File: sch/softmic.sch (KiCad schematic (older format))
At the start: 86 parts, among them J1 USB-C Connector, J2 XLR-OUT, J3 AudioJack 3.5mm, P1 4V1, P10 VccPad, P2 4V1, P3 4V1, P4 none, P5 none, P6 none, P7 none, P8 4V1, P9 4V1, Q1 MCP1812BT-033, Q10 ESP32-WROOM, Q11 BC847BS-TP, Q2 MMBFJ201, Q3 CH340G, Q4 BSS64AT116, Q5 OPA1671, Q6 OPA1671, Q7 BQ21040, Q8 MAX11613, Q9 Oled_128_32, SW1 RST, Y1 12MHz

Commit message: changed LED to red 0805 led
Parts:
- C1, C11, C12, C21, C22, C23, C24, C25, C3, C4, C5, C6, C7: Description CAP CER 1uF 10V X7R 0805 -> CAP CER 1uF 100V X7S 0805; MPN none -> HMK212BC7105MGHT; Manufacturer none -> Taiyo; Mouser PN none -> 963-HMK212BC7105MGHT; Mouser Price none -> $0.40
- C10, C14, C8: Description CAP CER 47uF 10V 0805 -> CAP CER 1206 10VDC 47uF 20% X6S; MPN none -> LMK316BC6476ML-T; Manufacturer none -> Taiyo; Mouser PN none -> 963-LMK316BC6476ML-T; Mouser Price none -> $0.70
- C13, C2, C9: Description CAP CER 22pF 10V X7R 0805 -> CAP CER 22pF 100V X7R 0805
- C15, C16: Description CAP CER 1uF 100V X7R 0805 -> CAP CER 1uF 100V X7S 0805; MPN none -> HMK212BC7105MGHT; Manufacturer none -> Taiyo; Mouser PN none -> 963-HMK212BC7105MGHT; Mouser Price none -> $0.40
- C19, C20: Description CAP CER 5.1nF 10V X7R 0805 -> CAP CER 5.1nF 100V X7R 0805
- D2: footprint LED_SMD:LED_0603_1608Metric -> LED_SMD:LED_0805_2012Metric_Pad1.15x1.40mm_HandSolder; Description LED Green 0603 SMD -> LED Red 0805 SMD; Digikey PN 511-1584-1-ND -> 732-4984-1-ND; Digikey Price $0.42 -> $0.18; LCSC PN C205443 -> (none); LCSC Price $0.008745 -> (none); MPN none -> Wurth; Manufacturer none -> 150080RS75000; Mouser PN 755-SMLD12EN1WT86 -> 710-150080RS75000; Mouser Price $0.40 -> $0.20

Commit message: pcb components placed
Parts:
- added C4: 1u, Capacitor_SMD:C_0805_2012Metric_Pad1.15x1.40mm_HandSolder, symbol Device:C
- logo1: footprint Symbol:OSHW-Logo2_7.3x6mm_SilkScreen -> Symbol:OSHW-Logo2_9.8x8mm_SilkScreen
- renumbered C9 to C10, C10 to C11, C11 to C12, C12 to C13, C13 to C14, C14 to C15, C15 to C16, C16 to C17, C17 to C18, C18 to C19, C19 to C20, C20 to C21, C21 to C22, C22 to C23, C23 to C24, C24 to C25, C25 to C26, C4 to C5, C5 to C6, C6 to C7, C7 to C8, C8 to C9, Q9 to DIS1
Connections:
- wire segments 251 -> 253
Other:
- moved on the sheet: C5

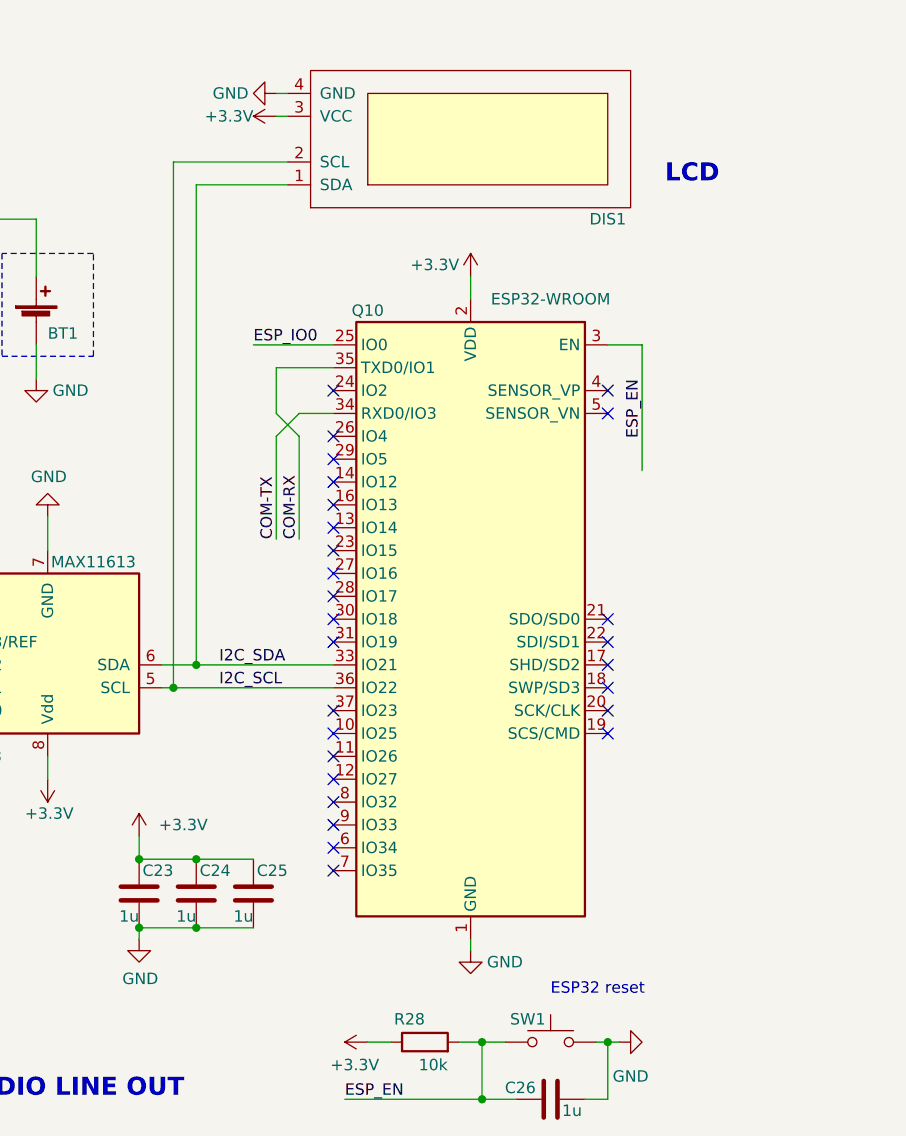
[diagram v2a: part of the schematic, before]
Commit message: changed ESP32 module for the 16MB version
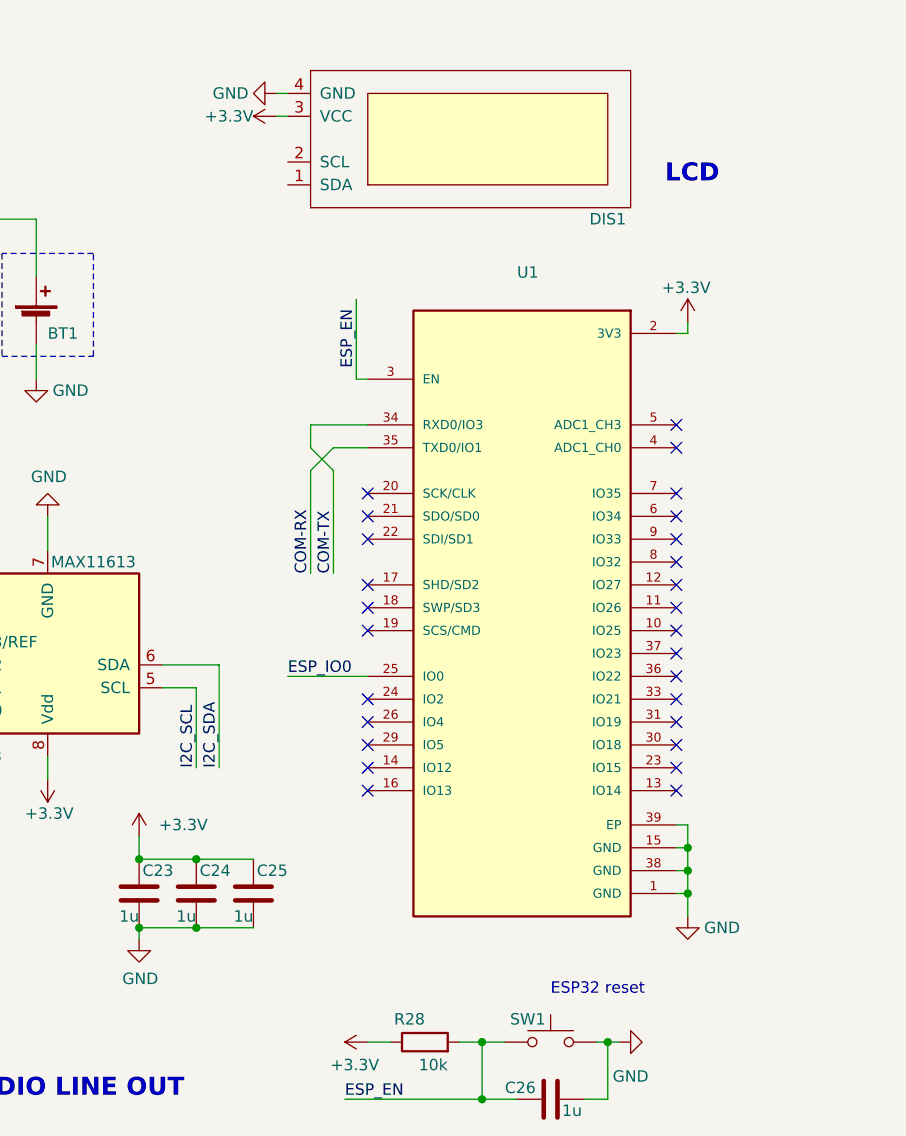
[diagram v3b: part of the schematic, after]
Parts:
- removed Q10: ESP32-WROOM, RF_Module:ESP32-WROOM-32, symbol RF_Module:ESP32-WROOM-32
- added U1: ESP32-WROVER-B 16MB, footprint:ESP32-WROVER-B_(16MB), symbol ESP32-WROVER-B.16MB:ESP32-WROVER-B_(16MB)
- Y1: Digikey Price (none) -> none; Mouser PN 717-AA-12.000MAGE-T -> 356-ESP32-WROB(16MB)
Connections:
- wire segments 253 -> 257
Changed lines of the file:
@@
 OP AMP 1\n
-$Comp
-L RF_Module:ESP32-WROOM-32 Q10
-U 1 1 5E8A3349
-P 9900 3050
-F 0 "Q10" H 10350 4400 50  0000 C CNN
-F 1 "ESP32-WROOM" H 9550 4450 50  0000 C CNN
-F 2 "RF_Module:ESP32-WROOM-32" H 9900 1550 50  0001 C CNN
-F 3 "https://www.espressif.com/sites/default/files/documentation/esp32-wroom-32_datasheet_en.pdf" H 9600 3100 50  0001 C CNN
-F 4 "Espressif Systems" H 9900 3050 50  0001 C CNN "Manufacturer"
-F 5 "ESP32-WROOM-32" H 9900 3050 50  0001 C CNN "MPN"
-F 6 "WiFi Modules (802.11) 4MB, ESP32-D0WDQ6" H 9900 3050 50  0001 C CNN "Description"
-F 7 "none" H 9900 3050 50  0001 C CNN "Digikey PN"
-F 8 "none" H 9900 3050 50  0001 C CNN "Digikey Price"
-F 9 "356-ESP-WROOM-32" H 9900 3050 50  0001 C CNN "Mouser PN"
-F 10 "$3.80" H 9900 3050 50  0001 C CNN "Mouser Price"
-F 11 "C95209" H 9900 3050 50  0001 C CNN "LCSC PN"
-F 12 "$2.79" H 9900 3050 50  0001 C CNN "LCSC Price"
-	1    9900 3050
-	-1   0    0    -1
-$EndComp
 $Comp
 L Device:C C21
@@
 L power:GND #PWR053
 U 1 1 5E85E862
-P 9900 4500
-F 0 "#PWR053" H 9900 4250 50  0001 C CNN
-F 1 "GND" H 9750 4450 50  0000 C CNN
-F 2 "" H 9900 4500 50  0001 C CNN
-F 3 "" H 9900 4500 50  0001 C CNN
-	1    9900 4500
+P 10850 4350
+F 0 "#PWR053" H 10850 4100 50  0001 C CNN
+F 1 "GND" H 10700 4300 50  0000 C CNN
+F 2 "" H 10850 4350 50  0001 C CNN
+F 3 "" H 10850 4350 50  0001 C CNN
+	1    10850 4350
 	-1   0    0    -1
 $EndComp
-Wire Wire Line
-	9900 4450 9900 4500
 $Comp
 L power:+3.3V #PWR052
 U 1 1 5E864686
-P 9900 1550
-F 0 "#PWR052" H 9900 1400 50  0001 C CNN
-F 1 "+3.3V" H 9950 1600 50  0000 L CNN
-F 2 "" H 9900 1550 50  0001 C CNN
-F 3 "" H 9900 1550 50  0001 C CNN
-	1    9900 1550
+P 10850 1750
+F 0 "#PWR052" H 10850 1600 50  0001 C CNN
+F 1 "+3.3V" H 10750 1900 50  0000 L CNN
+F 2 "" H 10850 1750 50  0001 C CNN
+F 3 "" H 10850 1750 50  0001 C CNN
+	1    10850 1750
 	-1   0    0    -1
 $EndComp
-Wire Wire Line
-	9900 1550 9900 1650
 Wire Wire Line
 	3400 6550 3300 6550
@@
 Wire Wire Line
 	8050 3750 8050 3650
-Text Label 8800 3350 0    50   ~ 0
+Text Label 8700 3700 1    50   ~ 0
 I2C_SCL
-Text Label 8800 3250 0    50   ~ 0
+Text Label 8800 3700 1    50   ~ 0
 I2C_SDA
 Wire Wire Line
@@
 Wire Wire Line
 	3950 4800 4300 4800
-NoConn ~ 9300 2050
-NoConn ~ 9300 2250
-NoConn ~ 9300 2350
-NoConn ~ 9300 2450
-NoConn ~ 9300 2650
-NoConn ~ 9300 2850
-NoConn ~ 9300 2950
-NoConn ~ 9300 3050
-NoConn ~ 9300 3150
-NoConn ~ 9300 3450
-NoConn ~ 9300 3550
-NoConn ~ 9300 3650
-NoConn ~ 9300 3750
-NoConn ~ 9300 3850
-NoConn ~ 9300 3950
-NoConn ~ 9300 4050
-NoConn ~ 9300 4150
-NoConn ~ 10500 3050
-NoConn ~ 10500 3150
-NoConn ~ 10500 3250
-NoConn ~ 10500 3350
-NoConn ~ 10500 3450
-NoConn ~ 10500 3550
-NoConn ~ 10500 2050
-NoConn ~ 10500 2150
 $Comp
 L Connector:XLR3 J2
@@
 Wire Wire Line
 	9100 750  9050 750
-Text Label 10650 2000 3    50   ~ 0
+Text Label 9400 1950 1    50   ~ 0
 ESP_EN
-NoConn ~ 9300 2750
-NoConn ~ 9300 2550
 $Comp
 L Switch:SW_Push SW1
@@
 	10500 5150 10500 4900
 Connection ~ 10500 4900
-Text Label 8950 1850 0    50   ~ 0
-ESP_IO0
-Wire Wire Line
-	8950 1850 9300 1850
-Wire Wire Line
-	10500 1850 10650 1850
+Wire Wire Line
+	9450 2000 9400 2000
 Wire Wire Line
 	3500 4800 3650 4800
@@
 Wire Wire Line
 	6950 3450 7550 3450
-Wire Wire Line
-	8600 1050 9100 1050
 Text Notes 10750 1150 0    79   ~ 16
 LCD\n
 Wire Wire Line
-	8550 3250 8700 3250
-Wire Wire Line
-	8550 3350 8600 3350
-Wire Wire Line
-	8700 3250 8700 1150
-Connection ~ 8700 3250
-Wire Wire Line
-	8700 3250 9300 3250
-Wire Wire Line
-	8700 1150 9100 1150
-Connection ~ 8600 3350
-Wire Wire Line
-	8600 3350 9300 3350
-Wire Wire Line
-	10650 1850 10650 2400
+	9400 2000 9400 1650
 Wire Wire Line
 	3300 4400 3800 4400
@@
 Text Label 3400 1150 0    50   ~ 0
 COM-TX
-Text Label 9150 2700 1    50   ~ 0
+Text Label 9200 2850 1    50   ~ 0
 COM-RX
-Text Label 9050 2700 1    50   ~ 0
+Text Label 9300 2850 1    50   ~ 0
 COM-TX
-Wire Wire Line
-	9300 2150 9150 2150
-Wire Wire Line
-	9300 1950 9050 1950
 Text Label 2900 3600 0    50   ~ 0
 JFET_OUT
@@
 	6850 6550 6850 7050
 Connection ~ 6050 6550
-Wire Wire Line
-	8600 1050 8600 3350
 Text Notes 7100 6850 0    79   ~ 16
 SOFTWARE-DEFINED WIRELESS MICROPHONE
@@
 ESP_EN
 Wire Wire Line
-	9150 2150 9050 2250
-Wire Wire Line
-	9050 2150 9150 2250
-Wire Wire Line
-	9050 1950 9050 2150
-Wire Wire Line
-	9150 2250 9150 2700
-Wire Wire Line
-	9050 2250 9050 2700
+	9300 2300 9200 2400
+Wire Wire Line
+	9200 2300 9300 2400
+Wire Wire Line
+	9200 2200 9200 2300
+Wire Wire Line
+	9300 2400 9300 2850
+Wire Wire Line
+	9200 2400 9200 2850
 Text Label 9300 5900 0    50   ~ 0
 RTS
@@
 F 7 "TCX Corporation" H 3800 2300 50  0001 C CNN "MPN"
 F 8 "AA-12.000MAGE-T " H 3800 2300 50  0001 C CNN "Manufacturer"
-F 9 "717-AA-12.000MAGE-T " H 3800 2300 50  0001 C CNN "Mouser PN"
+F 9 "356-ESP32-WROB(16MB) " H 3800 2300 50  0001 C CNN "Mouser PN"
 F 10 "$0.6" H 3800 2300 50  0001 C CNN "Mouser Price"
 F 11 " 887-1656-2-ND" H 3800 2300 50  0001 C CNN "Digikey PN"
+F 12 "none" H 3800 2300 50  0001 C CNN "Digikey Price"
 	1    3800 2300
 	1    0    0    -1
@@
 Wire Wire Line
 	2050 2350 2050 2300
+$Comp
+L ESP32-WROVER-B.16MB:ESP32-WROVER-B_(16MB) U1
+U 1 1 5EB184CB
+P 10150 3000
+F 0 "U1" H 10150 4467 50  0000 C CNN
+F 1 "ESP32-WROVER-B 16MB" V 10200 2250 50  0001 C CNN
+F 2 "footprint:ESP32-WROVER-B_(16MB)" H 10150 3000 50  0001 L BNN
+F 3 "https://eu.mouser.com/datasheet/2/891/esp32-wrover-b_datasheet_en-1384674.pdf" H 10150 3000 50  0001 L BNN
+F 4 "none" H 10150 3000 50  0001 C CNN "LCSC PN"
+F 5 "none" H 10150 3000 50  0001 C CNN "LCSC Price"
+F 6 "ESP32-WROVER-B (16MB)" H 10150 3000 50  0001 C CNN "MPN"
+F 7 "Espressif Systems" H 10150 3000 50  0001 C CNN "Manufacturer"
+F 8 "356-ESP32-WROB(16MB)" H 10150 3000 50  0001 C CNN "Mouser PN"
+F 9 "$4.80" H 10150 3000 50  0001 C CNN "Mouser Price"
+F 10 "ESP32 module M213DH2864PH3Q0, ESP32-D0WD, 64Mbits PSRAM, 16MB SPI flash, PCB Antenna" H 10150 3000 50  0001 C CNN "Description"
+F 11 "none" H 10150 3000 50  0001 C CNN "Digikey PN"
+F 12 "none" H 10150 3000 50  0001 C CNN "Digikey Price"
+	1    10150 3000
+	1    0    0    -1
+$EndComp
+Wire Wire Line
+	10800 1800 10850 1800
+Wire Wire Line
+	10850 1800 10850 1750
+Wire Wire Line
+	9450 2300 9300 2300
+Wire Wire Line
+	9450 2200 9200 2200
+Wire Wire Line
+	9100 3300 9450 3300
+Text Label 9100 3300 0    50   ~ 0
+ESP_IO0
+Wire Wire Line
+	10800 4250 10850 4250
+Wire Wire Line
+	10850 4250 10850 4350
+Wire Wire Line
+	10800 4150 10850 4150
+Wire Wire Line
+	10850 4150 10850 4250
+Connection ~ 10850 4250
+Wire Wire Line
+	10800 4050 10850 4050
+Wire Wire Line
+	10850 4050 10850 4150
+Connection ~ 10850 4150
+Wire Wire Line
+	10800 3950 10850 3950
+Wire Wire Line
+	10850 3950 10850 4050
+Connection ~ 10850 4050
+Wire Wire Line
+	8550 3350 8700 3350
+Wire Wire Line
+	8700 3350 8700 3700
+Wire Wire Line
+	8800 3250 8800 3700
+Wire Wire Line
+	8550 3250 8800 3250
+NoConn ~ 10800 2200
+NoConn ~ 10800 2300
+NoConn ~ 10800 2500
+NoConn ~ 10800 2600
+NoConn ~ 10800 2700
+NoConn ~ 10800 2800
+NoConn ~ 10800 2900
+NoConn ~ 10800 3000
+NoConn ~ 10800 3100
+NoConn ~ 10800 3200
+NoConn ~ 10800 3300
+NoConn ~ 10800 3400
+NoConn ~ 10800 3500
+NoConn ~ 10800 3600
+NoConn ~ 10800 3700
+NoConn ~ 10800 3800
+NoConn ~ 9450 3800
+NoConn ~ 9450 3700
+NoConn ~ 9450 3600
+NoConn ~ 9450 3500
+NoConn ~ 9450 3400
+NoConn ~ 9450 3100
+NoConn ~ 9450 3000
+NoConn ~ 9450 2900
+NoConn ~ 9450 2700
+NoConn ~ 9450 2600
+NoConn ~ 9450 2500
 $EndSCHEMATC
